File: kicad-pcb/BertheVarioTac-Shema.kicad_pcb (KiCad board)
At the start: 2 copper layers, 86 x 50 mm, 17 parts, among them CN1 Temperature and humidity inte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, P1 Power supply base, P3 Extended IO, P4 SPEAK, P5 10 k ohms, SW1 SW_DIP_x01

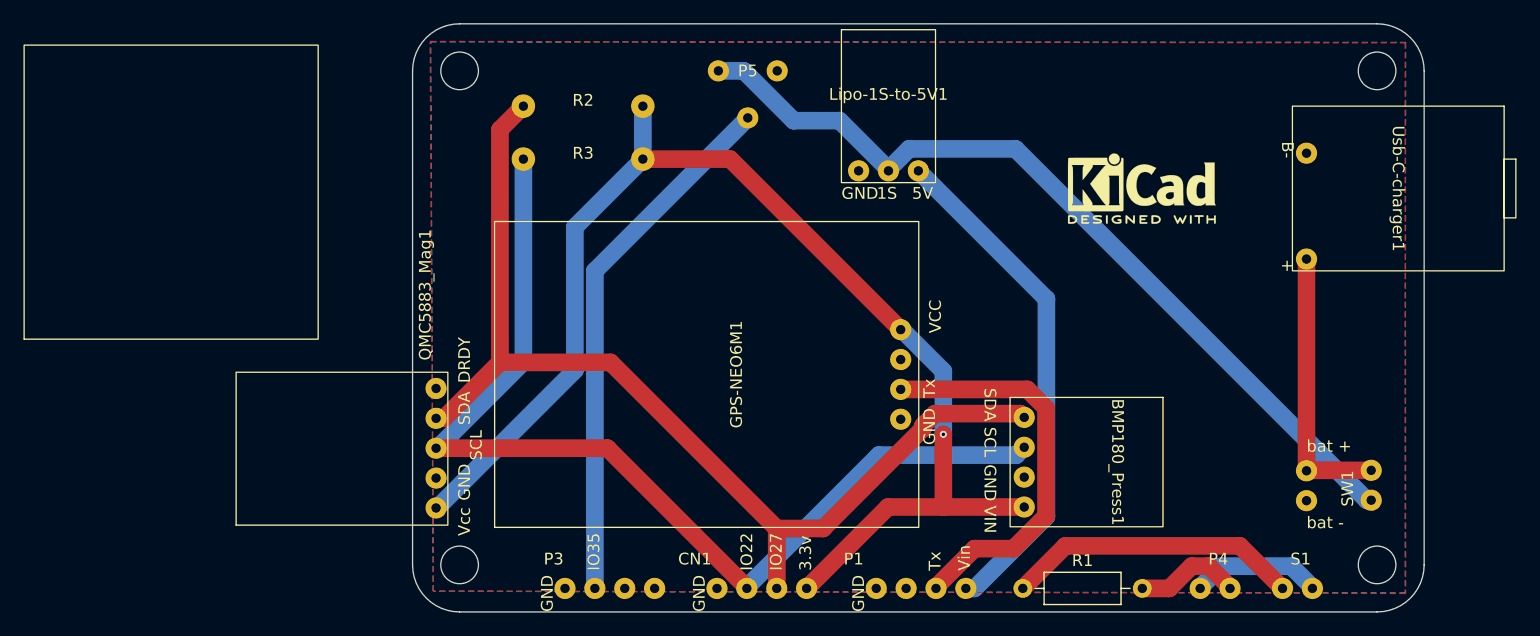
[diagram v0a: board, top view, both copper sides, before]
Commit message: modif pcb batterie
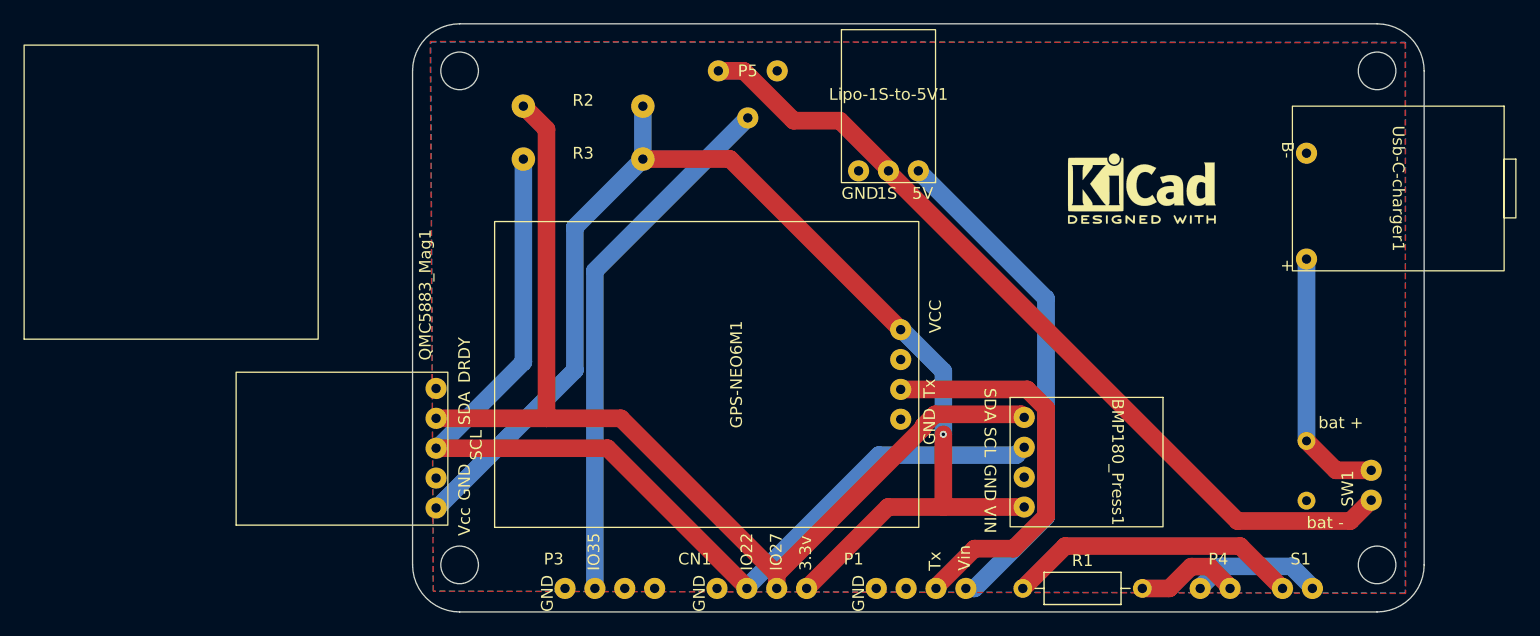
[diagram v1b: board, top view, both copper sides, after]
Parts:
- BT1: footprint BertheShema:2 trous standard -> BertheShema:batterie
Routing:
- net Net-(BT1-+): track 23.5 -> 22.0 mm
